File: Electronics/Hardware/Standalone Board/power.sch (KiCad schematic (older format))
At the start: 0 parts

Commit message: Add debug uart, gps uart, fan control and sdcard
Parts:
- added J?: BATT, symbol Connector:Conn_01x02_Female
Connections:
- new net +BATT: J?.2 (Pin_2)
- new net GND: J?.1 (Pin_1)
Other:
- note added: "TODO :\nReverse polarity protection"
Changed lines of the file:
@@
 $Descr A4 11693 8268
 encoding utf-8
-Sheet 1 7
+Sheet 6 7
 Title ""
 Date ""
@@
 Comment4 ""
 $EndDescr
+$Comp
+L Connector:Conn_01x02_Female J?
+U 1 1 5E2AE00C
+P 10100 1350
+F 0 "J?" H 10128 1326 50  0000 L CNN
+F 1 "BATT" H 10128 1235 50  0000 L CNN
+F 2 "" H 10100 1350 50  0001 C CNN
+F 3 "~" H 10100 1350 50  0001 C CNN
+	1    10100 1350
+	1    0    0    -1
+$EndComp
+$Comp
+L power:GND #PWR?
+U 1 1 5E2AE368
+P 9900 1350
+F 0 "#PWR?" H 9900 1100 50  0001 C CNN
+F 1 "GND" V 9905 1222 50  0000 R CNN
+F 2 "" H 9900 1350 50  0001 C CNN
+F 3 "" H 9900 1350 50  0001 C CNN
+	1    9900 1350
+	0    1    1    0
+$EndComp
+$Comp
+L power:+BATT #PWR?
+U 1 1 5E2AE701
+P 9900 1450
+F 0 "#PWR?" H 9900 1300 50  0001 C CNN
+F 1 "+BATT" V 9915 1577 50  0000 L CNN
+F 2 "" H 9900 1450 50  0001 C CNN
+F 3 "" H 9900 1450 50  0001 C CNN
+	1    9900 1450
+	0    -1   -1   0
+$EndComp
+Text Notes 9650 1200 0    50   ~ 0
+TODO :\nReverse polarity protection
+$Comp
+L power:+12V #PWR?
+U 1 1 5E2B0382
+P 9150 1050
+F 0 "#PWR?" H 9150 900 50  0001 C CNN
+F 1 "+12V" H 9165 1223 50  0000 C CNN
+F 2 "" H 9150 1050 50  0001 C CNN
+F 3 "" H 9150 1050 50  0001 C CNN
+	1    9150 1050
+	1    0    0    -1
+$EndComp
 $EndSCHEMATC

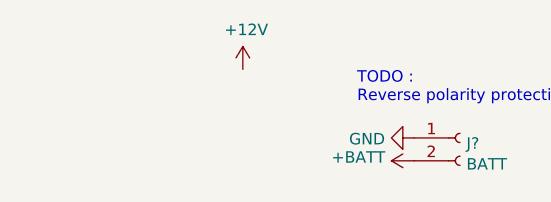
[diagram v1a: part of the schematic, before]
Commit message: Add rtc, pcie + mipi dsi high level connection, usb 2.0, usb 3.0 and remove audio section
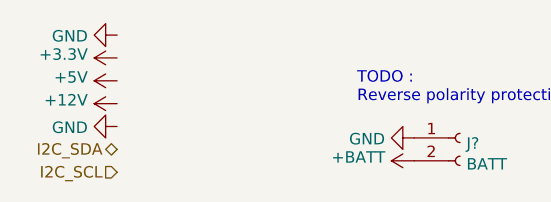
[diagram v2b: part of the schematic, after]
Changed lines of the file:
@@
 EESchema Schematic File Version 4
-LIBS:Standalone Board-cache
 EELAYER 30 0
 EELAYER END
 $Descr A4 11693 8268
 encoding utf-8
-Sheet 6 7
+Sheet 5 6
 Title ""
 Date ""
@@
 TODO :\nReverse polarity protection
 $Comp
+L power:GND #PWR?
+U 1 1 5DFA6ECC
+P 8600 900
+AR Path="/5DF06080/5DFA6ECC" Ref="#PWR?"  Part="1"
+AR Path="/5DF7A2D8/5DFA6ECC" Ref="#PWR?"  Part="1"
+F 0 "#PWR?" H 8600 650 50  0001 C CNN
+F 1 "GND" V 8605 772 50  0000 R CNN
+F 2 "" H 8600 900 50  0001 C CNN
+F 3 "" H 8600 900 50  0001 C CNN
+	1    8600 900
+	0    1    1    0
+$EndComp
+$Comp
+L power:+3.3V #PWR?
+U 1 1 5DFA6ED2
+P 8600 1000
+AR Path="/5DF06080/5DFA6ED2" Ref="#PWR?"  Part="1"
+AR Path="/5DF7A2D8/5DFA6ED2" Ref="#PWR?"  Part="1"
+F 0 "#PWR?" H 8600 850 50  0001 C CNN
+F 1 "+3.3V" V 8615 1128 50  0000 L CNN
+F 2 "" H 8600 1000 50  0001 C CNN
+F 3 "" H 8600 1000 50  0001 C CNN
+	1    8600 1000
+	0    -1   -1   0
+$EndComp
+$Comp
+L power:+5V #PWR?
+U 1 1 5DFA6ED8
+P 8600 1100
+AR Path="/5DF06080/5DFA6ED8" Ref="#PWR?"  Part="1"
+AR Path="/5DF7A2D8/5DFA6ED8" Ref="#PWR?"  Part="1"
+F 0 "#PWR?" H 8600 950 50  0001 C CNN
+F 1 "+5V" V 8615 1228 50  0000 L CNN
+F 2 "" H 8600 1100 50  0001 C CNN
+F 3 "" H 8600 1100 50  0001 C CNN
+	1    8600 1100
+	0    -1   -1   0
+$EndComp
+$Comp
 L power:+12V #PWR?
-U 1 1 5E2B0382
-P 9150 1050
-F 0 "#PWR?" H 9150 900 50  0001 C CNN
-F 1 "+12V" H 9165 1223 50  0000 C CNN
-F 2 "" H 9150 1050 50  0001 C CNN
-F 3 "" H 9150 1050 50  0001 C CNN
-	1    9150 1050
-	1    0    0    -1
+U 1 1 5DFA6EDE
+P 8600 1200
+AR Path="/5DF06080/5DFA6EDE" Ref="#PWR?"  Part="1"
+AR Path="/5DF7A2D8/5DFA6EDE" Ref="#PWR?"  Part="1"
+F 0 "#PWR?" H 8600 1050 50  0001 C CNN
+F 1 "+12V" V 8615 1328 50  0000 L CNN
+F 2 "" H 8600 1200 50  0001 C CNN
+F 3 "" H 8600 1200 50  0001 C CNN
+	1    8600 1200
+	0    -1   -1   0
+$EndComp
+Text HLabel 8600 1400 0    50   BiDi ~ 0
+I2C_SDA
+Text HLabel 8600 1500 0    50   Input ~ 0
+I2C_SCL
+$Comp
+L power:GND #PWR?
+U 1 1 5E00FF20
+P 8600 1300
+AR Path="/5DF06080/5E00FF20" Ref="#PWR?"  Part="1"
+AR Path="/5DF7A2D8/5E00FF20" Ref="#PWR?"  Part="1"
+F 0 "#PWR?" H 8600 1050 50  0001 C CNN
+F 1 "GND" V 8605 1172 50  0000 R CNN
+F 2 "" H 8600 1300 50  0001 C CNN
+F 3 "" H 8600 1300 50  0001 C CNN
+	1    8600 1300
+	0    1    1    0
 $EndComp
 $EndSCHEMATC

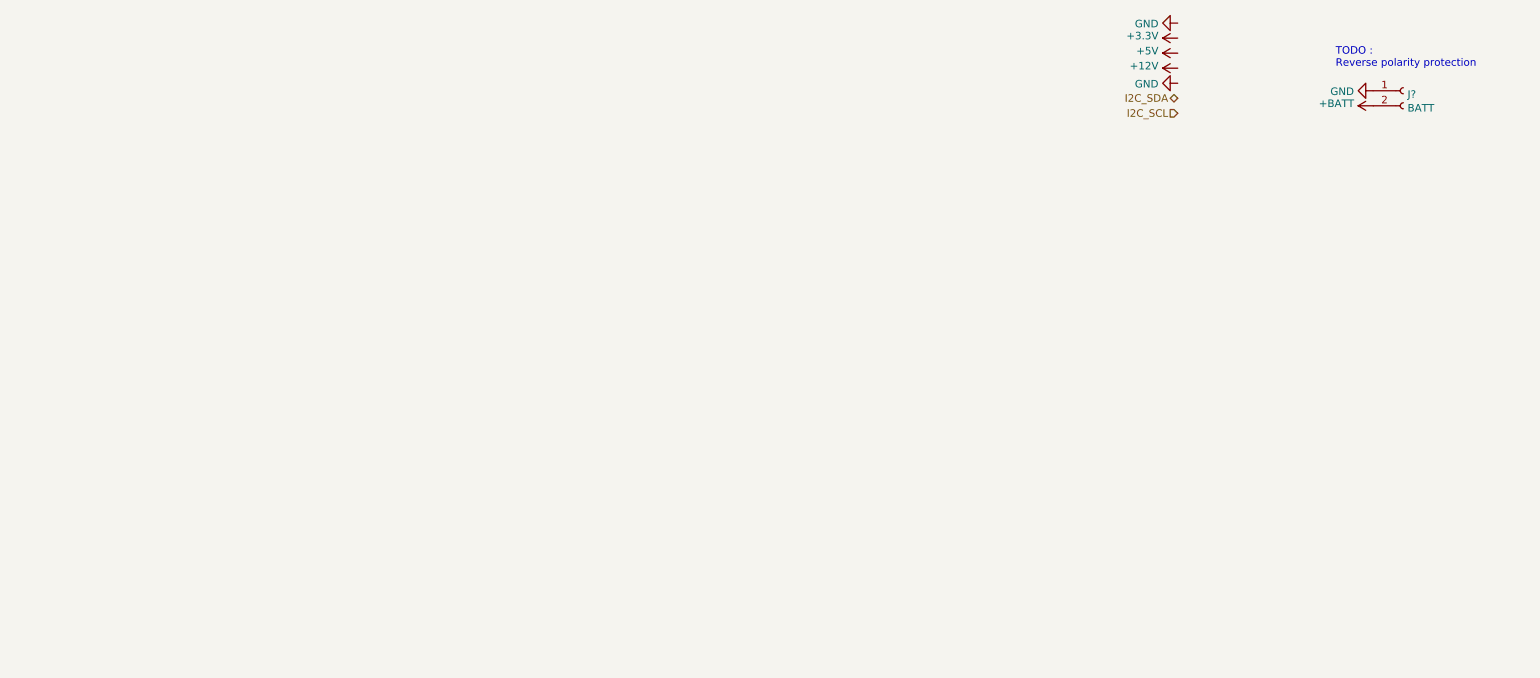
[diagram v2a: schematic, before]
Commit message: Fix all i2c voltage, add power/reset/recovery button, Mipi dsi hig level, add 3.0/3.3/5/1.1 volt power rail
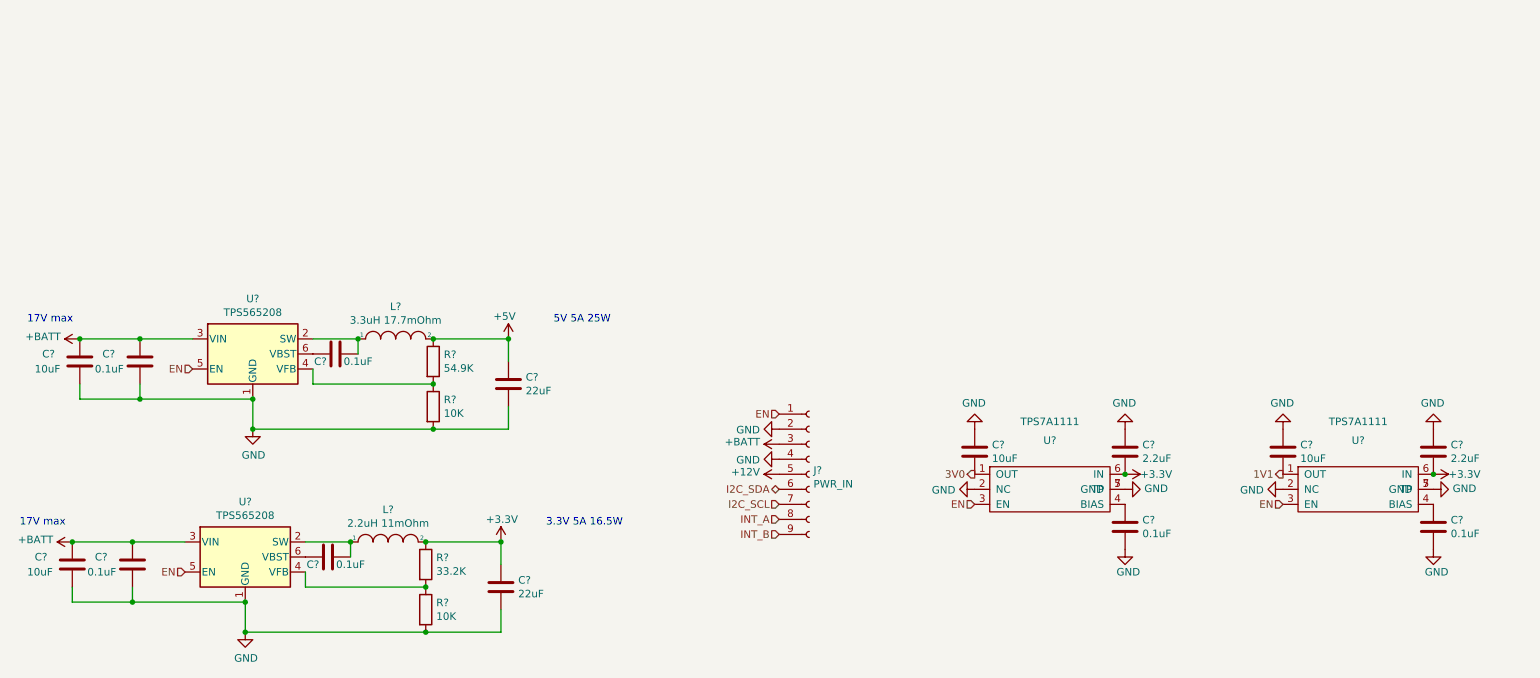
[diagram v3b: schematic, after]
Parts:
- removed J?: BATT, symbol Connector:Conn_01x02_Female
- added C? (x4): 10uF, symbol Device:C
- added C? (x6): 0.1uF, symbol Device:C
- added C? (x2): 22uF, symbol Device:C
- added C? (x2): 2.2uF, symbol Device:C
- added J?: PWR_IN, symbol Connector:Conn_01x09_Female
- added L?: 3.3uH 17.7mOhm, symbol pspice:INDUCTOR
- added L?: 2.2uH 11mOhm, symbol pspice:INDUCTOR
- added R?: 54.9K, symbol Device:R
- added R? (x2): 10K, symbol Device:R
- added R?: 33.2K, symbol Device:R
- added U? (x2): TPS565208, Package_TO_SOT_SMD:SOT-23-6, symbol Regulator_Switching:TPS565208
- added U? (x2): TPS7A1111, symbol sb:TPS7A11
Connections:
- net +12V: now also J?.5 (Pin_5)
- net +3V3: now also C?.1, C?.2, C?.2, L?.2, R?.1, U?.6 (IN), U?.6 (IN)
- net +5V: now also C?.1, L?.2, R?.1
- net +BATT: now also C?.1, C?.1, C?.1, C?.1, J?.3 (Pin_3), U?.3 (VIN), U?.3 (VIN)
- net GND: now also C?.1, C?.1, C?.1, C?.1, C?.2, C?.2, C?.2, C?.2, C?.2, C?.2, C?.2, C?.2, J?.2 (Pin_2), J?.4 (Pin_4), R?.2, R?.2, U?.1 (GND), U?.1 (GND), U?.2 (NC), U?.2 (NC), U?.5 (GND), U?.5 (GND), U?.7 (TP), U?.7 (TP)
- net I2C_SCL: now also J?.7 (Pin_7)
- net I2C_SDA: now also J?.6 (Pin_6)
- new net: C?.1, L?.1, U?.2 (SW) (x2)
- new net: R?.1, R?.2, U?.4 (VFB) (x2)
- new net: C?.2, U?.6 (VBST) (x2)
- new net: C?.1, U?.4 (BIAS) (x2)
- new net 1V1: C?.2, U?.1 (OUT)
- new net 3V0: C?.2, U?.1 (OUT)
- new net EN: J?.1 (Pin_1), U?.3 (EN), U?.3 (EN), U?.5 (EN), U?.5 (EN)
- new net INT_A: J?.8 (Pin_8)
- new net INT_B: J?.9 (Pin_9)
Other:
- note added: "17V max"
- note added: "3.3V 5A 16.5W"
- note added: "5V 5A 25W"
- note removed: "TODO :\nReverse polarity protection"

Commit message: Everything is routed, TODO : lenghtmatching + impedance matching + cleaning
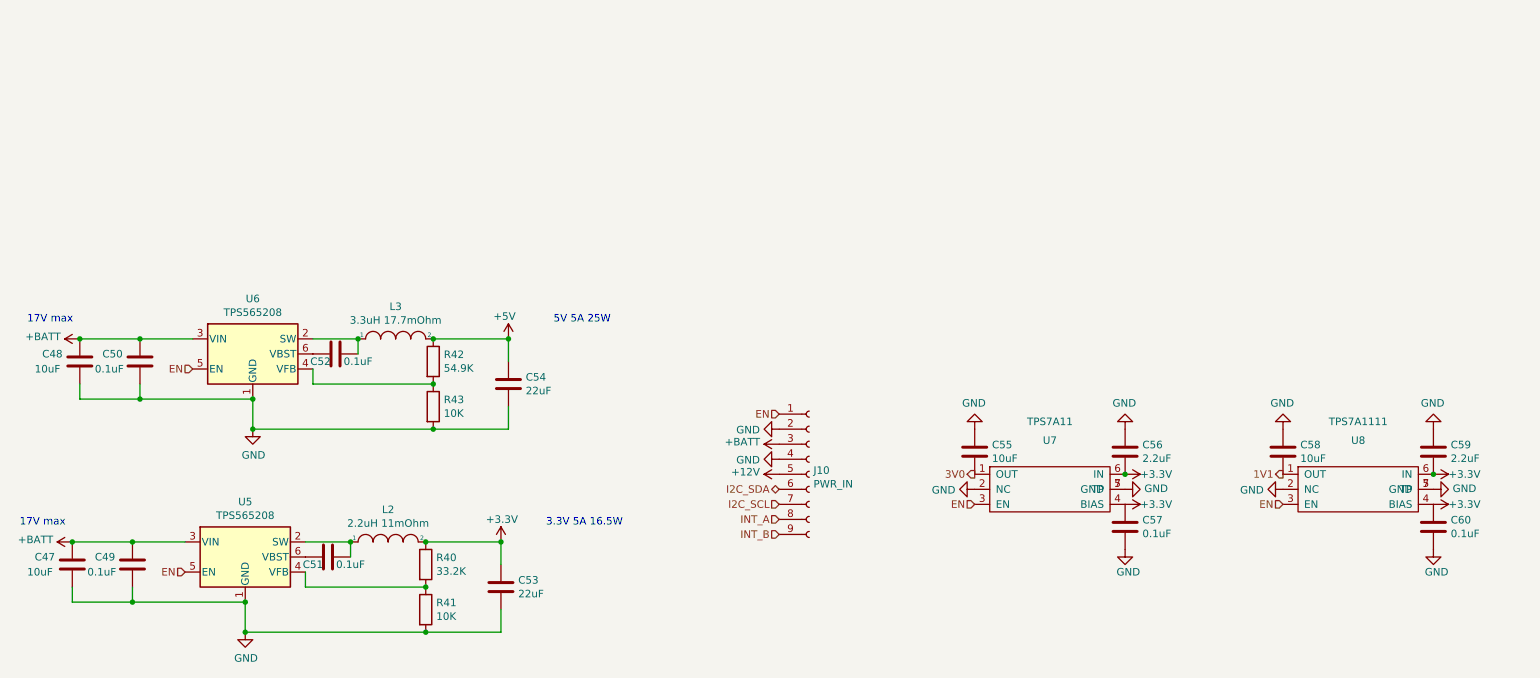
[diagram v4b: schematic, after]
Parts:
- C47, C48, C49, C50, C51, C52, C53, C54, C55, C56, C57, C58, C59, C60: renamed from C?; footprint (none) -> Capacitor_SMD:C_0402_1005Metric
- J10: renamed from J?; footprint (none) -> Connector_PinHeader_1.00mm:PinHeader_1x09_P1.00mm_Vertical
- L2, L3: renamed from L?; footprint (none) -> sb:DRA74
- R40, R41, R42, R43: renamed from R?; footprint (none) -> Resistor_SMD:R_0201_0603Metric
- U7: renamed from U?; value TPS7A1111 -> TPS7A11; footprint (none) -> Package_SON:WSON-6-1EP_2x2mm_P0.65mm_EP1x1.6mm
- U8: renamed from U?; footprint (none) -> Package_SON:WSON-6-1EP_2x2mm_P0.65mm_EP1x1.6mm
- gave numbers to parts that had none: 2
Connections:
- net +3V3: now also C57.1, C60.1, U7.4 (BIAS), U8.4 (BIAS)
